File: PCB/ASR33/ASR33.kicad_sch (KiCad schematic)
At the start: 44 parts, among them J1 Shelly, J2 DC, J3 Power, J4 RUN, J5 Tx, J6 Rx, J7 USB-C, Q1 NX7002AK, SW1 SW_Push, U1 ESP32-PICO-MINI-02, U2 FT231XQ, U3 NCR402U, U4 NCR402U, U5 LTV-356T, U6 LMR16006XDDCR, U7 QR

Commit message: Tidy
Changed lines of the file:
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@@
   (junction (at 34.29 39.37) (diameter 0) (color 0 0 0 0)
   )
-  (junction (at 148.082 63.5) (diameter 0) (color 0 0 0 0)
-  )
   (junction (at 73.66 48.26) (diameter 0) (color 0 0 0 0)
   )
@@
   (junction (at 60.96 129.54) (diameter 0) (color 0 0 0 0)
   )
-  (junction (at 170.942 43.18) (diameter 0) (color 0 0 0 0)
-  )
   (junction (at 225.425 36.83) (diameter 0) (color 0 0 0 0)
   )
@@
   (junction (at 45.72 137.16) (diameter 0) (color 0 0 0 0)
   )
-  (junction (at 170.942 33.02) (diameter 0) (color 0 0 0 0)
-  )
-  (junction (at 170.942 40.64) (diameter 0) (color 0 0 0 0)
-  )
   (junction (at 73.66 45.72) (diameter 0) (color 0 0 0 0)
   )
-  (junction (at 170.942 25.4) (diameter 0) (color 0 0 0 0)
-  )
   (junction (at 95.25 167.64) (diameter 0) (color 0 0 0 0)
   )
-  (junction (at 170.942 30.48) (diameter 0) (color 0 0 0 0)
-  )
   (junction (at 73.66 43.18) (diameter 0) (color 0 0 0 0)
   )
+  (junction (at 155.575 63.5) (diameter 0) (color 0 0 0 0)
+  )
   (junction (at 248.92 142.24) (diameter 0) (color 0 0 0 0)
   )
@@
   )
   (junction (at 180.975 31.75) (diameter 0) (color 0 0 0 0)
-  )
-  (junction (at 155.702 63.5) (diameter 0) (color 0 0 0 0)
   )
   (no_connect (at 177.8 106.68))
@@
     (stroke (width 0) (type default))
   )
-  (wire (pts (xy 170.942 43.18) (xy 183.515 43.18))
-    (stroke (width 0) (type default))
-  )
   (wire (pts (xy 129.54 144.78) (xy 129.54 146.05))
     (stroke (width 0) (type default))
   )
-  (wire (pts (xy 170.815 40.64) (xy 170.942 40.64))
-    (stroke (width 0) (type default))
-  )
   (wire (pts (xy 191.135 25.4) (xy 191.135 30.48))
     (stroke (width 0) (type default))
@@
     (stroke (width 0) (type default))
   )
-  (wire (pts (xy 170.942 40.64) (xy 177.8 40.64))
+  (wire (pts (xy 170.815 40.64) (xy 177.8 40.64))
     (stroke (width 0) (type default))
   )
@@
     (stroke (width 0) (type default))
   )
+  (wire (pts (xy 170.815 43.18) (xy 183.515 43.18))
+    (stroke (width 0) (type default))
+  )
   (wire (pts (xy 249.555 118.745) (xy 259.08 118.745))
     (stroke (width 0) (type default))
   )
+  (wire (pts (xy 170.815 30.48) (xy 173.355 30.48))
+    (stroke (width 0) (type default))
+  )
   (wire (pts (xy 129.54 113.03) (xy 127 113.03))
     (stroke (width 0) (type default))
@@
     (stroke (width 0) (type default))
   )
-  (wire (pts (xy 155.702 63.5) (xy 177.8 63.5))
+  (wire (pts (xy 155.575 63.5) (xy 177.8 63.5))
     (stroke (width 0) (type default))
   )
@@
     (stroke (width 0) (type default))
   )
-  (wire (pts (xy 147.955 63.5) (xy 148.082 63.5))
-    (stroke (width 0) (type default))
-  )
-  (wire (pts (xy 170.942 30.48) (xy 173.355 30.48))
-    (stroke (width 0) (type default))
-  )
   (wire (pts (xy 245.11 121.285) (xy 259.08 121.285))
     (stroke (width 0) (type default))
@@
     (stroke (width 0) (type default))
   )
-  (wire (pts (xy 170.815 30.48) (xy 170.942 30.48))
-    (stroke (width 0) (type default))
-  )
-  (wire (pts (xy 170.815 33.02) (xy 170.942 33.02))
-    (stroke (width 0) (type default))
-  )
-  (wire (pts (xy 170.942 33.02) (xy 173.355 33.02))
-    (stroke (width 0) (type default))
-  )
-  (wire (pts (xy 170.942 25.4) (xy 186.055 25.4))
+  (wire (pts (xy 170.815 33.02) (xy 173.355 33.02))
     (stroke (width 0) (type default))
   )
@@
     (stroke (width 0) (type default))
   )
-  (wire (pts (xy 170.815 43.18) (xy 170.942 43.18))
-    (stroke (width 0) (type default))
-  )
   (wire (pts (xy 220.98 36.83) (xy 225.425 36.83))
     (stroke (width 0) (type default))
@@
     (stroke (width 0) (type default))
   )
-  (wire (pts (xy 148.082 63.5) (xy 155.702 63.5))
+  (wire (pts (xy 147.955 63.5) (xy 155.575 63.5))
     (stroke (width 0) (type default))
   )
@@
     (stroke (width 0) (type default))
   )
-  (wire (pts (xy 170.815 25.4) (xy 170.942 25.4))
+  (wire (pts (xy 170.815 25.4) (xy 186.055 25.4))
     (stroke (width 0) (type default))
   )
@@
     )
   )
-  (symbol (lib_id "RevK:USB-C") (at 155.702 40.64 0) (unit 1)
-    (in_bom yes) (on_board yes) (dnp no)
-    (property "Reference" "J7" (at 158.4198 18.6182 0)
-      (effects (font (size 1.27 1.27)))
-    )
-    (property "Value" "USB-C" (at 158.4198 20.9296 0)
-      (effects (font (size 1.27 1.27)))
-    )
-    (property "Footprint" "RevK:USC16-TR" (at 155.702 20.32 0)
-      (effects (font (size 1.27 1.27)) hide)
-    )
-    (property "Datasheet" "https://www.usb.org/sites/default/files/documents/usb_type-c.zip" (at 155.702 17.78 0)
-      (effects (font (size 1.27 1.27)) hide)
-    )
-    (property "LCSC Part #" "C709357" (at 155.702 40.64 0)
-      (effects (font (size 1.27 1.27)) hide)
-    )
+  (symbol (lib_id "RevK:USB-C") (at 155.575 40.64 0) (unit 1)
+    (in_bom yes) (on_board yes) (dnp no)
+    (property "Reference" "J7" (at 158.2928 18.6182 0)
+      (effects (font (size 1.27 1.27)))
+    )
+    (property "Value" "USB-C" (at 158.2928 20.9296 0)
+      (effects (font (size 1.27 1.27)))
+    )
+    (property "Footprint" "RevK:USC16-TR" (at 155.575 20.32 0)
+      (effects (font (size 1.27 1.27)) hide)
+    )
+    (property "Datasheet" "https://www.usb.org/sites/default/files/documents/usb_type-c.zip" (at 155.575 17.78 0)
+      (effects (font (size 1.27 1.27)) hide)
+    )
+    (property "LCSC Part #" "C709357" (at 155.575 40.64 0)
+      (effects (font (size 1.27 1.27)) hide)
+    )

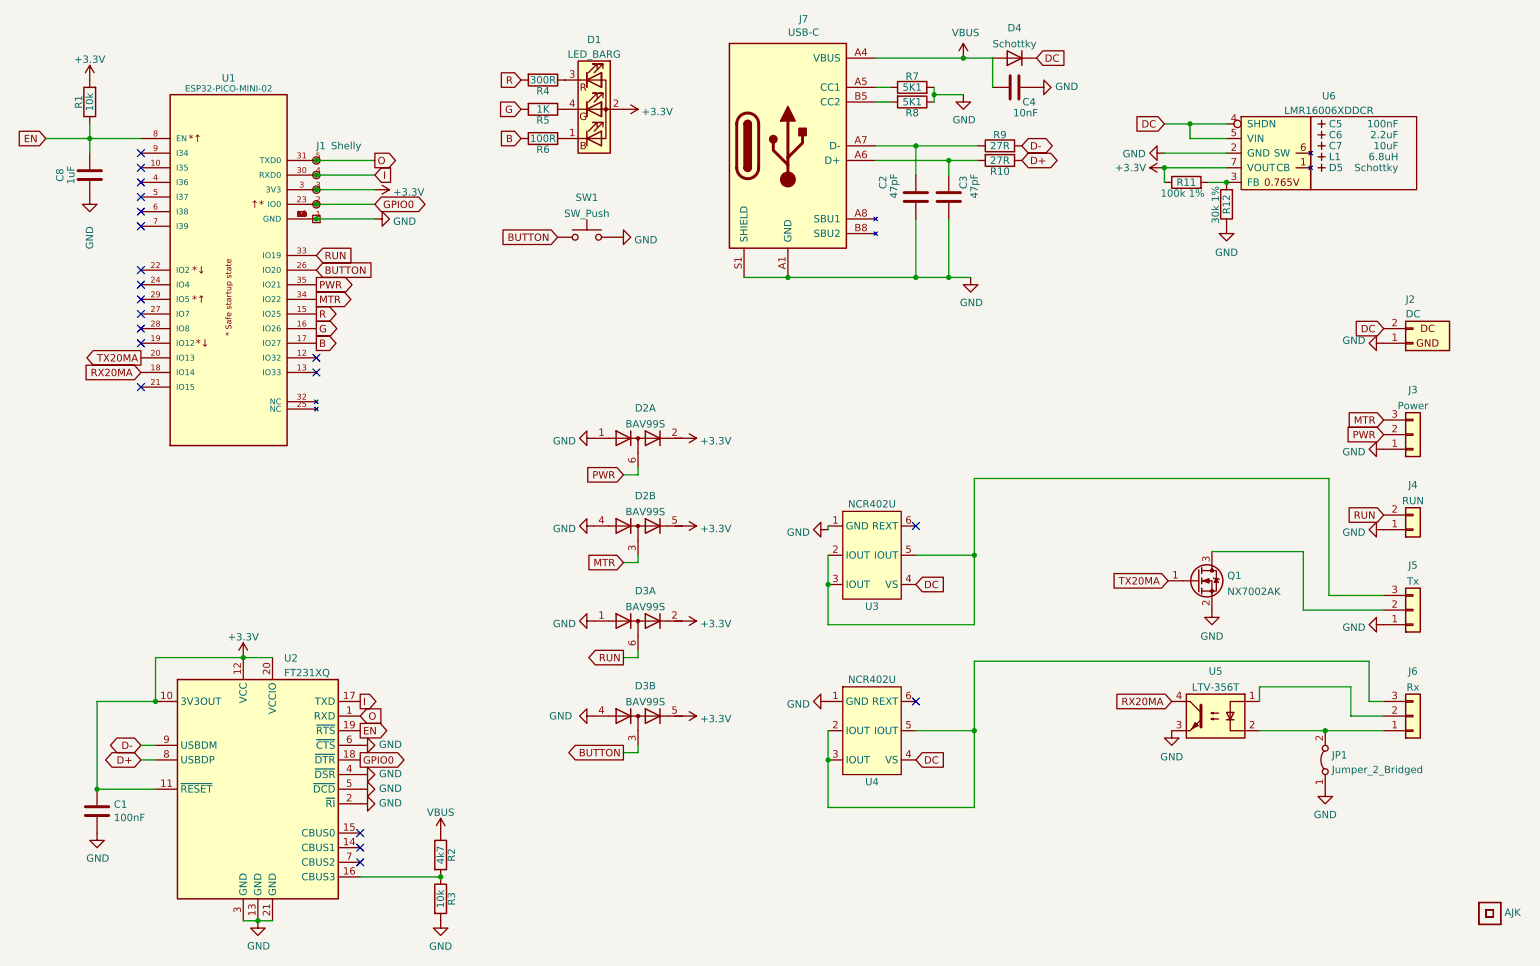
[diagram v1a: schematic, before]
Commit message: New layout with S3
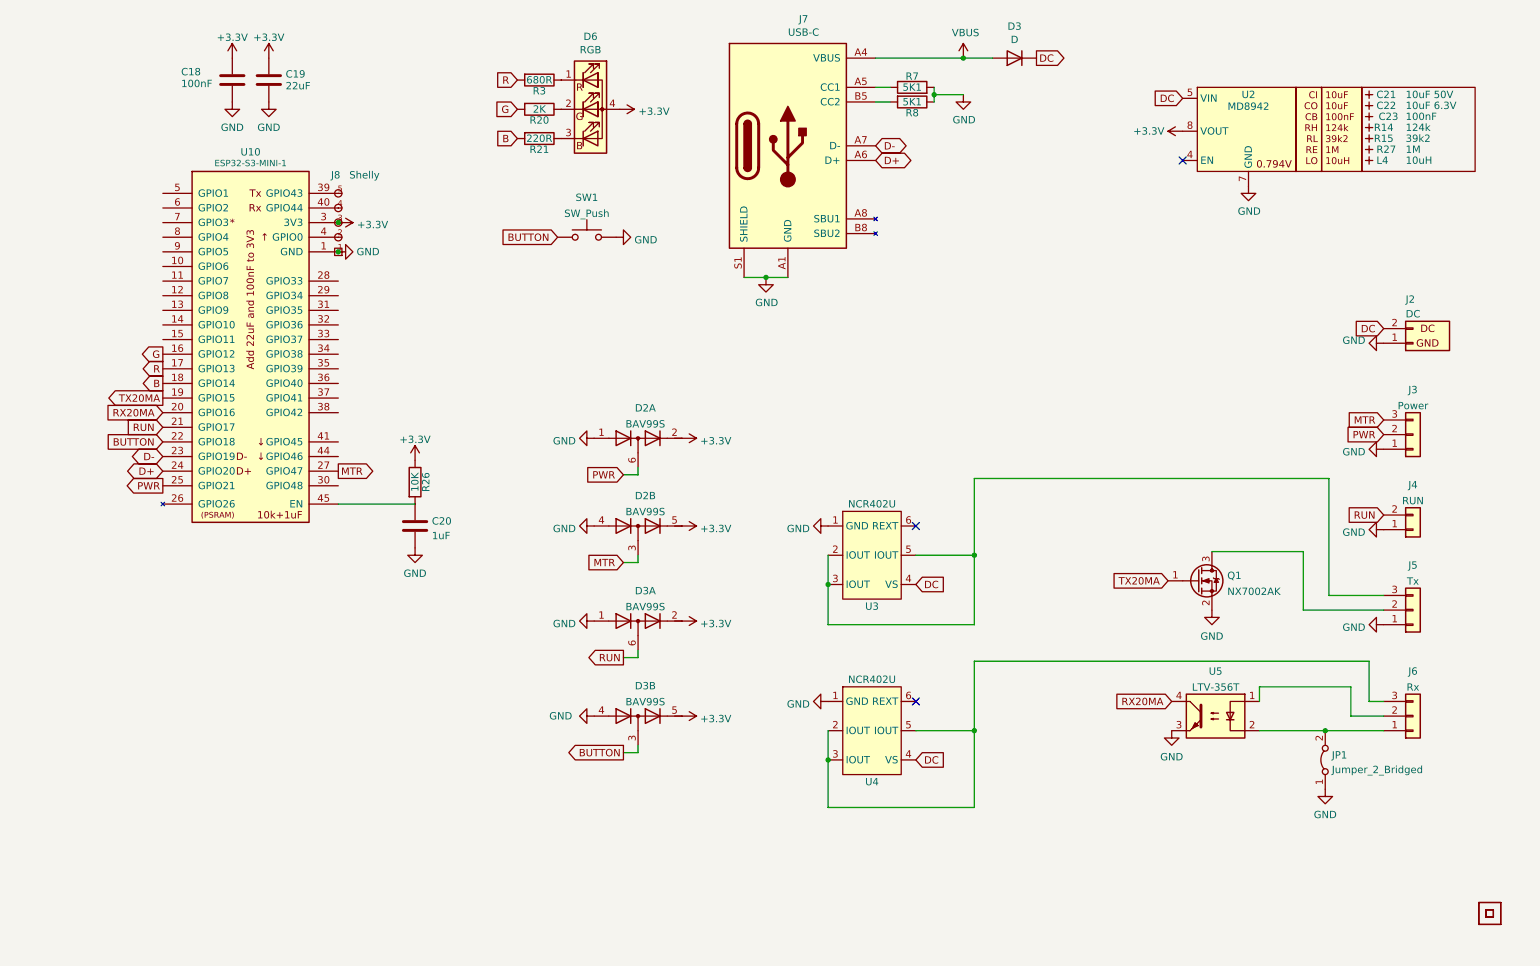
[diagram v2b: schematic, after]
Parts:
- removed C1: 100nF, RevK:C_0603, symbol Device:C
- removed C2, C3: 47pF, RevK:C_0603, symbol Device:C
- removed C4: 10nF, RevK:C_0603, symbol Device:C
- removed C5: 100nF, RevK:C_0603_, symbol RevK:Hidden
- removed C6: 2.2uF, RevK:C_0805_, symbol RevK:Hidden
- removed C7: 10uF, RevK:C_0805_, symbol RevK:Hidden
- removed C8: 1uF, RevK:C_0603, symbol Device:C
- removed D1: LED_BARG, RevK:MHS190RGBCT, symbol Device:LED_BARG
- removed D4: Schottky, RevK:D_1206, symbol Device:D
- removed D5: Schottky, RevK:D_1206_, symbol RevK:Hidden
- removed J1: Shelly, RevK:Shelly, symbol RevK:Shelly
- removed L1: 6.8uH, RevK:L_4x4_, symbol RevK:Hidden
- removed Logo1: AJK, RevK:AJK, symbol RevK:AJK
- removed R1: 10k, RevK:R_0603, symbol Device:R
- removed R10, R9: 27R, RevK:R_0603, symbol Device:R
- removed R11: 100k 1%, RevK:R_0603, symbol Device:R
- removed R12: 30k 1%, RevK:R_0603, symbol Device:R
- removed R2: 4k7, RevK:R_0603, symbol Device:R
- removed R4: 300R, RevK:R_0603, symbol Device:R
- removed R5: 1K, RevK:R_0603, symbol Device:R
- removed R6: 100R, RevK:R_0603, symbol Device:R
- removed U1: ESP32-PICO-MINI-02, RevK:ESP32-PICO-MINI-02, symbol RevK:ESP32-PICO-MINI-02
- removed U2: FT231XQ, RevK:QFN-20-1EP_4x4mm_P0.5mm_EP2.5x2.5mm, symbol RevK:FT231XQ
- removed U6: LMR16006XDDCR, RevK:SOT-23-Thin-6-Reg, symbol RevK:LMR16006XDDCR
- added C18: 100nF, RevK:C_0402, symbol Device:C
- added C19: 22uF, RevK:C_0402, symbol Device:C
- added C20: 1uF, RevK:C_0402, symbol Device:C
- added C21: 10uF 50V, RevK:C_0603_, symbol RevK:Hidden
- added C22: 10uF 6.3V, RevK:C_0603_, symbol RevK:Hidden
- added C23: 100nF, RevK:C_0603_, symbol RevK:Hidden
- added D3: D, RevK:D_SOD-123, symbol Device:D
- added D6: RGB, RevK:LED-RGB-1.6x1.6, symbol Device:LED_RGBA
- added J8: Shelly, RevK:Shelly, symbol RevK:Shelly
- added L4: 10uH, RevK:L_4x4_, symbol RevK:Hidden
- added R14: 124k, RevK:R_0402_, symbol RevK:Hidden
- added R15: 39k2, RevK:R_0402_, symbol RevK:Hidden
- added R20: 2K, RevK:R_0402, symbol Device:R
- added R21: 220R, RevK:R_0402, symbol Device:R
- added R26: 10K, RevK:R_0402, symbol Device:R
- added R27: 1M, RevK:R_0402_, symbol RevK:Hidden
- added U10: ESP32-S3-MINI-1, RevK:ESP32-S3-MINI-1, symbol RevK:ESP32-S3-MINI-1-N4R2
- added U2: MD8942, RevK:SOT-23-6-MD8942, symbol RevK:MD89420-RegBlock
- D2, D3: footprint Package_TO_SOT_SMD:SOT-363_SC-70-6 -> RevK:SOT-363_SC-70-6
- R3: value 10k -> 680R; footprint RevK:R_0603 -> RevK:R_0402
- R7, R8: footprint RevK:R_0603 -> RevK:R_0402
- SW1: footprint RevK:SW_PUSH_6mm_PTH -> RevK:TS-1092S-B3D2-G
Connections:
- net +3V3: now also C18.1, C19.1, D6.4 (A), J8.3 (3V3), R26.1, U10.3 (3V3), U2.8 (VOUT)
- net B: now also R21.2, U10.18 (GPIO14)
- net BUTTON: now also U10.22 (GPIO18)
- net D+: now also J7.A6 (D+), J7.B6 (D+), U10.24 (GPIO20)
- net D-: now also J7.A7 (D-), J7.B7 (D-), U10.23 (GPIO19)
- net DC: now also D3.1 (K), U2.5 (VIN)
- net G: now also R20.2, U10.16 (GPIO12)
- net GND: now also C18.2, C19.2, C20.2, J8.1 (GND), U10.1 (GND), U10.2 (GND), U10.42 (GND), U10.43 (GND), U10.46 (GND), U10.47 (GND), U10.48 (GND), U10.49 (GND), U10.50 (GND), U10.51 (GND), U10.52 (GND), U10.53 (GND), U10.54 (GND), U10.55 (GND), U10.56 (GND), U10.57 (GND), U10.58 (GND), U10.59 (GND), U10.60 (GND), U10.61 (GND), U10.62 (GND), U10.63 (GND), U10.64 (GND), U10.65 (GND), U2.2 (GND), U2.7 (GND); no longer R3.2
- net MTR: now also U10.27 (GPIO47)
- net PWR: now also U10.25 (GPIO21)
- net R: now also R3.2, U10.17 (GPIO13)
- net RUN: now also U10.21 (GPIO17)
- net RX20MA: now also U10.20 (GPIO16)
- net TX20MA: now also U10.19 (GPIO15)
- net VBUS: now also D3.2 (A)
- net at R3.1: now also D6.1 (RK)
- new net: D6.2 (GK), R20.1
- new net: C20.1, R26.2, U10.45 (EN)
- new net: D6.3 (BK), R21.1
- new net: J8.2 (0), U10.4 (GPIO0)
- new net: J8.4 (Rx), U10.40 (GPIO44)
- new net: J8.5 (Tx), U10.39 (GPIO43)
- no-connect marks 20 -> 3

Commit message: Clean up PCB
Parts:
- removed D2, D3: BAV99S, RevK:SOT-363_SC-70-6, symbol Diode:BAV99S
- removed unit 2 of D3
- removed D6: RGB, RevK:LED-RGB-1.6x1.6, symbol Device:LED_RGBA
- removed J7: USB-C, RevK:USC16-TR, symbol RevK:USB-C
- removed R20: 2K, RevK:R_0402, symbol Device:R
- removed R21: 220R, RevK:R_0402, symbol Device:R
- removed R3: 680R, RevK:R_0402, symbol Device:R
- added D1: XL-1010RGBC-WS2812B, RevK:SMD1010, symbol RevK:WS2812B-1mm
- added D2, D3, D6, D7: ~, RevK:DFN1006-2L, symbol RevK:ES05D1MC10
- added J7: USB-C-Socket-V, RevK:USB-C-Socket-H, symbol RevK:USB-C-Socket-H
- added PCB1: 70x70, RevK:PCB7070, symbol RevK:PCB
- added V1, V2, V3, V4: ~, RevK:VCUT70N, symbol RevK:VCUT
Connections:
- net +3V3: now also D1.2 (+)
- net BUTTON: now also D2.1
- net D+: now also J7.A6 (D+), J7.B6 (D+)
- net D-: now also J7.A7 (D-), J7.B7 (D-)
- net GND: now also D1.3 (-), D2.2, D3.2, D6.2, D7.2, J7.A1 (GND), J7.A12 (GND), J7.B1 (GND), J7.B12 (GND), J7.S1 (SHIELD)
- net MTR: now also D6.1
- net PWR: now also D3.1
- net RUN: now also D7.1
- net VBUS: now also J7.A4 (VBUS), J7.A9 (VBUS), J7.B4 (VBUS), J7.B9 (VBUS)
- net at R7.1: now also J7.A5 (CC1)
- net at R8.2: now also J7.B5 (CC2)
- net B: no longer names the net of U10.18 (GPIO14)
- net G renamed RGB
- net RGB: now also D1.4 (I)
- net R: no longer names the net of U10.17 (GPIO13)
- no-connect marks 3 -> 30
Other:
- moved on the sheet: J2, J3, J4

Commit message: Tweak
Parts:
- C21: value 10uF 50V -> 10uF 35V; LCSC Part # C1591 -> C194427
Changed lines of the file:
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@@
       (effects (font (size 1.27 1.27)) (justify left))
     )
-    (property "Value" "10uF 50V" (at 262.89 31.75 0)
+    (property "Value" "10uF 35V" (at 262.89 31.75 0)
       (effects (font (size 1.27 1.27)) (justify left))
     )
@@
       (effects (font (size 1.27 1.27)) hide)
     )
-    (property "LCSC Part #" "C1591" (at 256.54 31.75 0)
+    (property "LCSC Part #" "C194427" (at 256.54 31.75 0)
       (effects (font (size 1.27 1.27)) hide)
     )

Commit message: Tidy
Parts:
- D1: footprint RevK:SMD1010 -> RevK:SMD1010+
- J2, J3, J4, J5, J6: now left out of the parts list
- R14: LCSC Part # (none) -> C138062
